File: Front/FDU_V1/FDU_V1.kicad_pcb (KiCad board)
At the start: 4 copper layers, 197.1 x 120.1 mm, 165 parts, among them IC1 SN65HVD230, IC10 XL1509-5.0E1, IC11 TDA2822D, IC12 AMS1117-3.3, IC2 WeMos_D1_mini, IC3 74LVC3G17DC,125, IC4 STM32F103RBT6, IC5 MCP6291T-E_OT, IC6 LM2901, IC7 CD74HC30M96, IC8 74LVC3G17DC,125, IC9 SN74LVC3G04DCUR, J1 SWPROG, X1 S3D4.000000B20F30T, Y1 8MHz

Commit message: Add V1 board
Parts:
- removed the IC4 at (59.7, 95.0)
- removed X1: S3D4.000000B20F30T, Oscillator:Oscillator_SMD_EuroQuartz_XO32-4Pin_3.2x2.5mm
- added C17: 1uF, Capacitor_SMD:C_0805_2012Metric, F.Cu at (236.6, 83.3)
- added C18: 1uF, Capacitor_SMD:C_0805_2012Metric, F.Cu at (173.0, 85.8)
- added C49: 0.1uF, Capacitor_SMD:C_0805_2012Metric, F.Cu at (147.1, 108.3)
- added C50: 0.1uF, Capacitor_SMD:C_0805_2012Metric, F.Cu at (144.6, 97.4)
- added C63: 0.1uF, Capacitor_SMD:C_0805_2012Metric, F.Cu at (84.0, 92.0)
- added D10: SMAJ18CA, Samacsys:DIONM5127X229N, F.Cu at (200.2, 87.8)
- added D15: SMAJ5.0A, Samacsys:DIOM5127X229N, F.Cu at (117.5, 117.1)
- added D17: ESDCAN01-2BLY, Samacsys:SOT95P255X150-3N, F.Cu at (165.8, 62.4)
- added D5: SMAJ5.0A, Samacsys:DIOM5127X229N, F.Cu at (235.4, 71.7)
- added IC13: SN74LVC1G125DCK, Package_TO_SOT_SMD:Texas_R-PDSO-G5_DCK-5, F.Cu at (79.7, 92.3)
- added IC7: STM32F103VCTx, Package_QFP:LQFP-100_14x14mm_P0.5mm, F.Cu at (158.3, 104.6)
- added J1: 12V TEST, Connector_PinHeader_2.54mm:PinHeader_1x02_P2.54mm_Vertical, F.Cu at (129.1, 69.5)
- added J2: WiFi serial interface, Connector_PinHeader_2.54mm:PinHeader_1x05_P2.54mm_Vertical, F.Cu at (172.2, 119.6)
- added J4: SWPROG, Connector_PinHeader_2.54mm:PinHeader_1x03_P2.54mm_Vertical, F.Cu at (178.5, 79.2)
- added JP1: Termination, Jumper:SolderJumper-2_P1.3mm_Open_RoundedPad1.0x1.5mm, F.Cu at (167.6, 67.7)
- added Q1: MMBT3904, Package_TO_SOT_SMD:SOT-23, F.Cu at (97.7, 85.7)
- added Q2: MMBT3904, Package_TO_SOT_SMD:SOT-23, F.Cu at (97.7, 80.3)
- added R23: 1K2, Resistor_SMD:R_0805_2012Metric, F.Cu at (158.8, 43.5)
- added R24: 1K2, Resistor_SMD:R_0805_2012Metric, F.Cu at (173.0, 78.5)
- added R26: 2K2, Resistor_SMD:R_0805_2012Metric, F.Cu at (173.0, 82.1)
- added R27: 10K, Resistor_SMD:R_0805_2012Metric, F.Cu at (236.7, 79.7)
- added R28: 1K, Resistor_SMD:R_0805_2012Metric, F.Cu at (144.6, 94.1)
- added R49: 0R, Resistor_SMD:R_0805_2012Metric, F.Cu at (152.1, 64.5)
- added R51: 1K, Resistor_SMD:R_0805_2012Metric, F.Cu at (100.0, 123.2)
- added R52: 2K, Resistor_SMD:R_0805_2012Metric, F.Cu at (100.0, 126.5)
- added R53: 120R, Resistor_SMD:R_0805_2012Metric, F.Cu at (167.6, 71.5)
- added R54: 4K7, Resistor_SMD:R_0805_2012Metric, F.Cu at (201.9, 90.8)
- added R55: 1K5, Resistor_SMD:R_0805_2012Metric, F.Cu at (201.9, 93.5)
- added R57: 27K, Resistor_SMD:R_0805_2012Metric, F.Cu at (109.9, 76.8)
- added R58: 1K, Resistor_SMD:R_0805_2012Metric, F.Cu at (92.7, 84.7)
- added R59: 1K, Resistor_SMD:R_0805_2012Metric, F.Cu at (92.7, 79.4)
- added R64: 3K9, Resistor_SMD:R_0805_2012Metric, F.Cu at (157.4, 125.0)
- added R65: 47K, Resistor_SMD:R_0805_2012Metric, F.Cu at (157.3, 121.5)
- added R71: 100R, Resistor_SMD:R_0805_2012Metric, F.Cu at (61.5, 72.5)
- added R72: 100R, Resistor_SMD:R_0805_2012Metric, F.Cu at (69.9, 153.1)
- added TP1: TestPoint, TestPoint:TestPoint_Loop_D2.50mm_Drill1.0mm, F.Cu at (167.9, 82.2)
- added TP10: TestPoint, TestPoint:TestPoint_Loop_D2.50mm_Drill1.0mm, F.Cu at (182.9, 149.8)
- added TP11: TestPoint, TestPoint:TestPoint_Loop_D2.50mm_Drill1.0mm, F.Cu at (171.9, 149.6)
- added TP12: TestPoint, TestPoint:TestPoint_Loop_D2.50mm_Drill1.0mm, F.Cu at (177.8, 149.7)
- added TP13: TestPoint, TestPoint:TestPoint_Loop_D2.50mm_Drill1.0mm, F.Cu at (85.7, 97.1)
- added TP14: TestPoint, TestPoint:TestPoint_Loop_D2.50mm_Drill1.0mm, F.Cu at (53.9, 100.1)
- added TP15: TestPoint, TestPoint:TestPoint_Loop_D2.50mm_Drill1.0mm, F.Cu at (70.7, 99.9)
- added TP16: TestPoint, TestPoint:TestPoint_Loop_D2.50mm_Drill1.0mm, F.Cu at (68.7, 79.7)
- added TP17: TestPoint, TestPoint:TestPoint_Loop_D2.50mm_Drill1.0mm, F.Cu at (56.0, 80.0)
- added TP18: TestPoint, TestPoint:TestPoint_Loop_D2.50mm_Drill1.0mm, F.Cu at (69.3, 42.1)
- added TP19: TestPoint, TestPoint:TestPoint_Loop_D2.50mm_Drill1.0mm, F.Cu at (129.4, 153.5)
- added TP2: TestPoint, TestPoint:TestPoint_Loop_D2.50mm_Drill1.0mm, F.Cu at (81.8, 128.2)
- added TP20: TestPoint, TestPoint:TestPoint_Loop_D2.50mm_Drill1.0mm, F.Cu at (200.4, 150.2)
- added TP21: TestPoint, TestPoint:TestPoint_Loop_D2.50mm_Drill1.0mm, F.Cu at (128.8, 42.6)
- added TP22: TestPoint, TestPoint:TestPoint_Loop_D2.50mm_Drill1.0mm, F.Cu at (128.8, 48.0)
- added TP23: TestPoint, TestPoint:TestPoint_Loop_D2.50mm_Drill1.0mm, F.Cu at (200.3, 142.0)
- added TP24: TestPoint, TestPoint:TestPoint_Loop_D2.50mm_Drill1.0mm, F.Cu at (57.3, 67.1)
- added TP3: TestPoint, TestPoint:TestPoint_Loop_D2.50mm_Drill1.0mm, F.Cu at (142.4, 151.2)
- added TP4: TestPoint, TestPoint:TestPoint_Loop_D2.50mm_Drill1.0mm, F.Cu at (105.0, 133.4)
- added TP5: TestPoint, TestPoint:TestPoint_Loop_D2.50mm_Drill1.0mm, F.Cu at (133.9, 44.6)
- added TP6: TestPoint, TestPoint:TestPoint_Loop_D2.50mm_Drill1.0mm, F.Cu at (104.4, 120.1)
- added TP7: TestPoint, TestPoint:TestPoint_Loop_D2.50mm_Drill1.0mm, F.Cu at (142.4, 144.3)
- added TP8: TestPoint, TestPoint:TestPoint_Loop_D2.50mm_Drill1.0mm, F.Cu at (148.9, 149.5)
- added TP9: TestPoint, TestPoint:TestPoint_Loop_D2.50mm_Drill1.0mm, F.Cu at (148.9, 144.2)
- C15: renamed from C8; value 10uF -> 10nF
- C44: renamed from C11; value 0.1uF -> 1uF 25V
- IC12: renamed from IC3; value 74LVC3G17DC,125 -> SN74LVC3G17DCTR; footprint Samacsys:SOP50P310X100-8N -> Package_SO:MSOP-8_3x3mm_P0.65mm
- IC2: value WeMos_D1_mini -> NCV8452STT3G; footprint Samacsys:SOIC127P600X175-8N -> Samascys:SOT230P700X180-4N
- R1: renamed from R16; value 10k -> 10K
- R10: renamed from R47; value 1.5K -> 1K5
- R11: renamed from R54; value 1.5K -> 1K5
- R12: renamed from R51; value 1.2K -> 1K2
- R13: renamed from R25; value 3.3K -> 1K8
- R14: renamed from R43; value 2.2K -> 2K2
- R17: renamed from R50; value 1.2K -> 10K
- R18: renamed from R26; value 3.3K -> 1K8
- R2: renamed from R20; value 10k -> 10K
- R22: renamed from R14; value 10k -> 2K2
- R25: renamed from R52; value 2.2K -> 1K2
- R29: renamed from R38; value 4.7K -> 4K7
- R3: value 1K -> 3K9
- R30: renamed from R45; value 4.7K -> 4K7
- R31: renamed from R42; value 1.5K -> 1K5
- R32: renamed from R48; value 1.5K -> 1K5
- R33: renamed from R30; value 10k -> 10K
- R39: renamed from R1; value 6.2K -> 6K2
- R4: renamed from R24; value 10K -> 3K9
- R40: renamed from R5; value 6.2K -> 6K2
- R42: renamed from R31; value 10k -> 10K
- R43: renamed from R2; value 2.6K -> 2K6
- R44: renamed from R6; value 2.6K -> 2K6
- R45: renamed from R36; value 10K -> 1K
- R46: value 10K -> 1K
- R47: renamed from R40; value 10K -> 1K
- R48: renamed from R49; value 10K -> 1K
- R5: renamed from R37; value 4.7K -> 4K7
- R6: renamed from R44; value 4.7K -> 4K7
- R66: renamed from R17; value 10k -> 10K
- R68: renamed from R9; value 6.8k -> 6K8
- R7: renamed from R53; value 4.7K -> 4K7
- R70: renamed from R10; value 5.1k -> 5K1
- R8: renamed from R39; value 1.2K -> 1K2
- R9: renamed from R41; value 1.5K -> 1K5
- moved C2 295.9 mm to (58.7, 108.5)
- moved IC1 295.4 mm to (69.9, 119.6)
- moved C25 295.2 mm to (80.2, 151.2), turned to 180 degrees
- moved IC11 292.4 mm to (64.8, 92.7)
- moved C11 290.3 mm to (63.7, 117.8), turned to 180 degrees
- moved LED1 288.4 mm to (79.4, 83.3)
- moved C22 287.1 mm to (80.3, 143.3), turned to 180 degrees
- moved C68 286.6 mm to (58.9, 96.0)
- moved C67 286.0 mm to (58.8, 91.4)
- moved R2 285.0 mm to (58.7, 104.9)
- moved C31 282.8 mm to (91.8, 152.5)
- moved R37 280.8 mm to (80.2, 147.6), turned to 180 degrees
- moved IC4 272.1 mm to (93.6, 119.4)
- moved C64 271.7 mm to (58.8, 87.0)
- moved C69 270.6 mm to (69.3, 91.8)
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- renumbered C22 to C1, C54 to C10, C32 to C11, C46 to C12, C35 to C13, C55 to C14, C33 to C16, C58 to C19, C28 to C2, C61 to C20, C52 to C21, C21 to C22, C24 to C23, C27 to C24, C30 to C25, C47 to C26, C31 to C27, C48 to C28, C49 to C29, C44 to C3, C53 to C30, C10 to C31, C13 to C32, C34 to C33, C20 to C34, C56 to C35, C62 to C36, C29 to C37, C9 to C38, C3 to C39, C57 to C4, C4 to C40, C15 to C41, C5 to C42, C6 to C43, C16 to C45, C7 to C46, C25 to C47, C12 to C48, C60 to C5, C36 to C51, C37 to C52, C1 to C53, C2 to C54, C26 to C55, C38 to C56, C39 to C57, C50 to C58, C40 to C59, C64 to C6, C51 to C60, C41 to C61, C42 to C62, C17 to C64, C43 to C65, C14 to C66, C18 to C67, C19 to C68, C23 to C69, C63 to C7, C45 to C8, C59 to C9, D9 to D1, D2 to D11, D3 to D12, D5 to D14, D4 to D16, D13 to D2, D7 to D3, D12 to D4, D8 to D6, D10 to D7, D11 to D8, D6 to D9, H3 to H2, H5 to H3, H7 to H4, H2 to H5, H4 to H6, H6 to H7, IC6 to IC1, IC12 to IC10, IC5 to IC11, IC11 to IC3, IC7 to IC4, IC1 to IC5, IC8 to IC6, IC10 to IC8, J1 to J3, D1 to LED2, R32 to R15, R34 to R16, R33 to R19, R35 to R20, R28 to R21, R15 to R34, R18 to R35, R19 to R36, R22 to R37, R23 to R38, R27 to R41, R21 to R50, R4 to R56, R13 to R60, R11 to R61, R12 to R62, R7 to R63, R8 to R67, R29 to R69
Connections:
- net Net-(IC4-VDDA) renamed +3V3A
- C15 pad 1: +5V -> Net-(IC4-F)
- C16 pad 1: +12V -> Net-(IC2-OUT)
- C3 pad 1: Net-(C44-Pad1) -> Net-(C3-Pad1)
- C33 pad 2: /EXCITER -> /EXCA
- C44 pad 1: +3V3 -> /T15_OUT
- C7 pad 1: /TMPM_IN -> /TMPM1_IN
- CONN1 pad 2: unconnected-(CONN1-Pin_2-Pad2) -> /HS_TEMP
- CONN1 pad 6: unconnected-(CONN1-Pin_6-Pad6) -> Net-(CONN1-Pin_6)
- CONN2 pad 2: unconnected-(CONN2-Pin_2-Pad2) -> Net-(CONN2-Pin_2)
- CONN3 pad 2: unconnected-(CONN3-Pin_2-Pad2) -> Net-(CONN3-Pin_2)
- CONN3 pad 6: unconnected-(CONN3-Pin_6-Pad6) -> Net-(CONN3-Pin_6)
- CONN4 pad 2: unconnected-(CONN4-Pin_2-Pad2) -> Net-(CONN4-Pin_2)
- CONN4 pad 8: unconnected-(CONN4-Pin_8-Pad8) -> Net-(CONN4-Pin_8)
- CONN5 pad 3: /LINK DISCH -> /LINK DISCH_OUT
- CONN6 pad 1: unconnected-(CONN6-Pad1) -> /CANH
- CONN6 pad 10: unconnected-(CONN6-Pad10) -> /MOT_TMP2
- CONN6 pad 11: unconnected-(CONN6-Pad11) -> /THROTTLE 2
- CONN6 pad 12: unconnected-(CONN6-Pad12) -> /THROTTLE 1
- CONN6 pad 14: unconnected-(CONN6-Pad14) -> /BRAKE
- CONN6 pad 15: unconnected-(CONN6-Pad15) -> /T15_IN
- CONN6 pad 16: unconnected-(CONN6-Pad16) -> +5V
- CONN6 pad 17: unconnected-(CONN6-Pad17) -> /EXCA
- CONN6 pad 18: unconnected-(CONN6-Pad18) -> /EXCB
- CONN6 pad 2: unconnected-(CONN6-Pad2) -> /CANL
- CONN6 pad 20: unconnected-(CONN6-Pad20) -> /RES_COSB
- CONN6 pad 21: unconnected-(CONN6-Pad21) -> /RES_COSA
- CONN6 pad 22: unconnected-(CONN6-Pad22) -> /CRUISE
- CONN6 pad 23: unconnected-(CONN6-Pad23) -> /RES_SINA
- CONN6 pad 24: unconnected-(CONN6-Pad24) -> /RES_SINB
- CONN6 pad 28: unconnected-(CONN6-Pad28) -> +12P
- CONN6 pad 29: unconnected-(CONN6-Pad29) -> +12P
- CONN6 pad 3: unconnected-(CONN6-Pad3) -> /START
- CONN6 pad 30: unconnected-(CONN6-Pad30) -> +12P
- CONN6 pad 31: unconnected-(CONN6-Pad31) -> +12P
- CONN6 pad 32: unconnected-(CONN6-Pad32) -> +12P
- CONN6 pad 33: unconnected-(CONN6-Pad33) -> +12P
- CONN6 pad 34: unconnected-(CONN6-Pad34) -> +12P
- CONN6 pad 35: unconnected-(CONN6-Pad35) -> +12P
- CONN6 pad 36: unconnected-(CONN6-Pad36) -> +12P
- CONN6 pad 37: unconnected-(CONN6-Pad37) -> +12P
- CONN6 pad 38: unconnected-(CONN6-Pad38) -> +12P
- CONN6 pad 39: unconnected-(CONN6-Pad39) -> +12P
- CONN6 pad 40: unconnected-(CONN6-Pad40) -> +12P
- CONN6 pad 41: unconnected-(CONN6-Pad41) -> +12P
- CONN6 pad 42: unconnected-(CONN6-Pad42) -> +12P
- CONN6 pad 43: unconnected-(CONN6-Pad43) -> +12P
- CONN6 pad 44: unconnected-(CONN6-Pad44) -> +12P
- CONN6 pad 45: unconnected-(CONN6-Pad45) -> +12P
- CONN6 pad 46: unconnected-(CONN6-Pad46) -> +12P
- CONN6 pad 47: unconnected-(CONN6-Pad47) -> +12P
- CONN6 pad 48: unconnected-(CONN6-Pad48) -> +12P
- CONN6 pad 49: unconnected-(CONN6-Pad49) -> +12P
- CONN6 pad 5: unconnected-(CONN6-Pad5) -> /WTR_TMP1
- CONN6 pad 50: unconnected-(CONN6-Pad50) -> +12P
- CONN6 pad 6: unconnected-(CONN6-Pad6) -> /WTR_TMP2
- CONN6 pad 7: unconnected-(CONN6-Pad7) -> /FORWARD
- CONN6 pad 8: unconnected-(CONN6-Pad8) -> /REVERSE
- CONN6 pad 9: unconnected-(CONN6-Pad9) -> /MOT_TMP1
- D1 pad 1: /REV_IN -> /REVERSE
- D2 pad 1: /START_IN -> /START
- D3 pad 1: /FWD_IN -> /FORWARD
- D4 pad 1: /TMPM_IN -> /MOT_TMP1
- D6 pad 1: /BRAKE_IN -> /BRAKE
- D7 pad 1: /CRUISE_IN -> /CRUISE
- D8 pad 1: /THROTTLE 2 IN -> /THROTTLE 2
- D9 pad 1: /THROTTLE 1 IN -> /THROTTLE 1
- IC1 pad 1: Net-(IC7-F) -> Net-(IC4-F)
- IC1 pad 13: Net-(IC7-F) -> Net-(IC4-F)
- IC1 pad 14: Net-(IC7-F) -> Net-(IC4-F)
- IC1 pad 2: Net-(IC7-F) -> Net-(IC4-F)
- IC12 pad 1: Net-(IC3-1A) -> /8Mhz Clock
- IC12 pad 2: unconnected-(IC3-3Y-Pad2) -> /LINK DISCH_OUT
- IC12 pad 6: GND -> /LINK DISCH
- IC2 pad 1: unconnected-(IC2-~{RST}-Pad1) -> Net-(IC2-OUT)
- IC2 pad 2: unconnected-(IC2-A0-Pad2) -> GND
- IC2 pad 3: unconnected-(IC2-D0-Pad3) -> Net-(IC2-IN)
- IC2 pad 4: unconnected-(IC2-SCK/D5-Pad4) -> +12V
- IC3 pad 2: +12V -> Net-(IC2-OUT)
- IC4 pad 6: Net-(IC7-F) -> Net-(IC4-F)
- IC4 pad 8: /BKIN -> Net-(IC4-~{Y})
- IC8 pad 4: GND -> Net-(IC8-ON/OFF)
- R12 pad 1: /TMPM_IN -> /TMPM1_IN
- R12 pad 2: /MOT_TMP2 -> /MOT_TMP1
- R13 pad 2: Net-(C44-Pad1) -> Net-(C3-Pad1)
- R17 pad 2: /MOT_TMP1 -> /TMPM1_IN
- R22 pad 1: Net-(IC7-F) -> Net-(IC4-F)
- R25 pad 1: /TMPM_IN -> /TMPM2_IN
- R25 pad 2: GND -> /MOT_TMP2
- R3 pad 1: Net-(IC4-PA0) -> Net-(C3-Pad1)
- R3 pad 2: +3V3 -> /HFEXC
- R4 pad 1: Net-(C44-Pad1) -> Net-(C3-Pad1)
- R47 pad 1: /THROTTLE 1 -> /THROTTLE 1 IN
- R48 pad 1: /THROTTLE 2 -> /THROTTLE 2 IN
- R56 pad 1: +3V3 -> GND
- R62 pad 1: GND -> /BMS_IN
- R62 pad 2: /BMS_IN -> GND
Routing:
- net GND: track 0.00 -> 252.1 mm, vias 0 -> 132
- net +12V: track 0.00 -> 213.8 mm, vias 0 -> 6
- net /TMPM2_IN: track 0.00 -> 185.4 mm, vias 0 -> 2
- net /MOT_TMP1: track 0.00 -> 175.0 mm, vias 0 -> 2
- net Net-(IC4-C): track 0.00 -> 173.5 mm
- net Net-(IC4-G): track 0.00 -> 162.6 mm, vias 0 -> 2
- net /IL1_IN: track 0.00 -> 158.5 mm, vias 0 -> 5
- net /T15_OUT: track 0.00 -> 157.9 mm, vias 0 -> 4
- net /BRAKE_IN: track 0.00 -> 157.5 mm, vias 0 -> 2
- net /IL2_IN: track 0.00 -> 157.5 mm, vias 0 -> 4
- net /THROTTLE 2: track 0.00 -> 147.8 mm, vias 0 -> 2
- net /OCUR_NEG: track 0.00 -> 139.4 mm, vias 0 -> 2
- net /PWM A LO: track 0.00 -> 136.1 mm, vias 0 -> 1
- net /PWM A HI: track 0.00 -> 134.4 mm, vias 0 -> 1
- net /REV_IN: track 0.00 -> 132.0 mm, vias 0 -> 3
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- added copper zone on F.Cu, net +3V3
- added copper zone on In3.Cu, net +3V3
- added copper zone on F.Cu, net +5V
- added copper zone on F.Cu, net GND
- added copper zone on F.Cu, net Net-(C56-Pad1)
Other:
- board size 197.1 x 120.1 mm -> 196 x 119 mm
- copper layers 4 -> 6
- board text added: "12V"
- board text added: "3V3 ON"
- board text added: "5V"
- board text added: "ACCTY"
- board text added: "BK"
- board text added: "C"
- board text added: "CH"
- board text added: "CL"
- board text added: "D"
- board text added: "EXC"
- board text added: "G"
- board text added: "GND"
- board text added: "HFEXC"
- board text added: "IL1"
- board text added: "IL2"
- board text added: "OC"
- board text added: "Rx"
- board text added: "SWPROG"
- board text added: "Tx"
- board text added: "WiFi"
- board text added: "iPACE INVERTER LOGIC BOARD V1 ©2026 D.MAGUIRE,J.HÜBNER,N.HEDLUND EVBMW.COM OPENINVERTER.ORG"
- board text removed: "iPACE FDU INVERTER LOGIC BOARD V1 ©2023 D.MAGUIRE , J.HÜBNER EVBMW.COM OPENINVERTER.ORG"

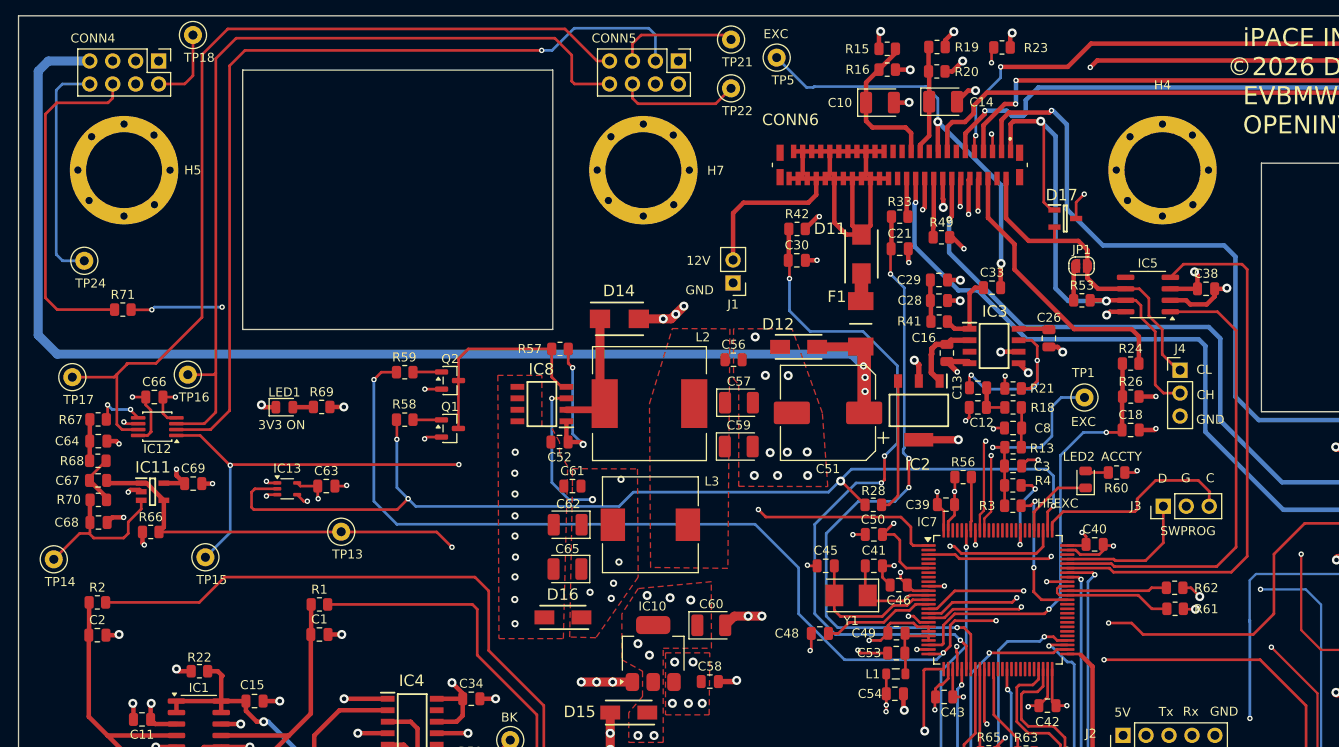
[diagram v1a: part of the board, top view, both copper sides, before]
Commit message: Update design as per order
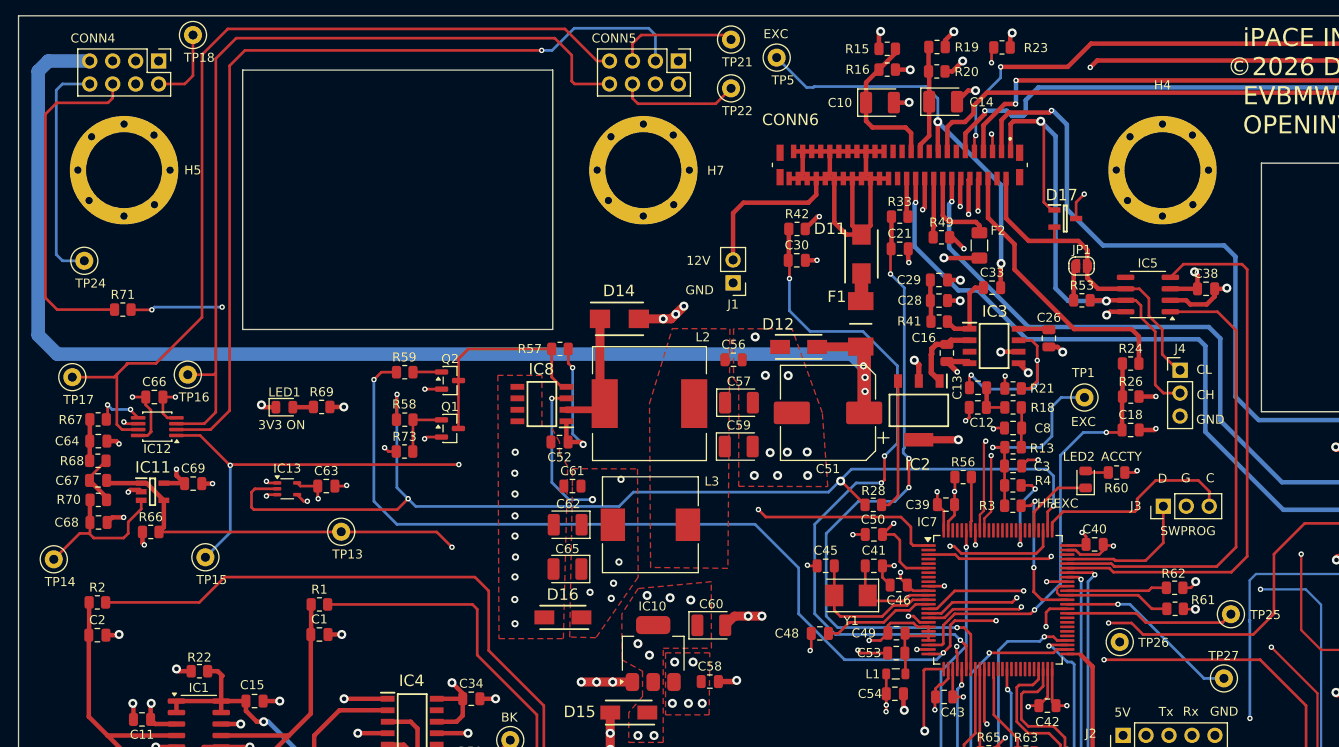
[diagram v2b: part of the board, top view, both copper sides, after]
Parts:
- added F2: 1206L050/24WR, Fuse:Fuse_1206_3216Metric, F.Cu at (156.3, 65.4)
- added R73: 10K, Resistor_SMD:R_0805_2012Metric, F.Cu at (92.7, 88.2)
- added TP25: TestPoint, TestPoint:TestPoint_Loop_D2.50mm_Drill1.0mm, F.Cu at (184.1, 106.2)
- added TP26: TestPoint, TestPoint:TestPoint_Loop_D2.50mm_Drill1.0mm, F.Cu at (171.8, 109.3)
- added TP27: TestPoint, TestPoint:TestPoint_Loop_D2.50mm_Drill1.0mm, F.Cu at (183.3, 113.3)
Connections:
- CONN6 pad 16: +5V -> Net-(CONN6-Pad16)
- IC7 pad 60: unconnected-(IC7-PD13-Pad60) -> Net-(IC7-PD13)
- IC7 pad 61: unconnected-(IC7-PD14-Pad61) -> Net-(IC7-PD14)
- IC7 pad 62: unconnected-(IC7-PD15-Pad62) -> Net-(IC7-PD15)
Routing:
- net Net-(IC7-PD15): track 0.00 -> 20.7 mm, vias 0 -> 1
- net Net-(IC7-PD13): track 0.00 -> 18.9 mm
- net Net-(IC7-PD14): track 0.00 -> 12.9 mm, vias 0 -> 1
- net Net-(CONN6-Pad16): track 0.00 -> 9.42 mm
- net /MAIN_PSU_EN: track 115.7 -> 121.4 mm
- net Net-(Q1-B): track 3.12 -> 6.62 mm
- net GND: track 252.1 -> 253.1 mm, vias 132 -> 133
- net /TMPWTR_IN: track 48.6 -> 47.7 mm
- net +5V: track 47.7 -> 48.4 mm
